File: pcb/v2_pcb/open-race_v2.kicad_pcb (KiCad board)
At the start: 8 copper layers, 90.5 x 49.5 mm, 337 parts, among them IC1 AP33772SDKZ-13-FA02, J1 Conn_ARM_SWD_TagConnect_TC203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, J2 USB4105-GF-A, J20 2S_PACK_BALANCE, J3 DM3CS-SF, J800 M50-3530642 (VTREF sense only), J900 U.FL-R-SMT-1(10), Q1 CSD18540Q5B, Q2 CSD18540Q5B, Q3 CSD18540Q5B, Q4 CSD18540Q5B, Q5 CSD18540Q5B, SW1101 KMR223NG ULC LFG, SW1102 KMR223NG ULC LFG, SW1103 KMR223NG ULC LFG, SW300 KMR223NG ULC LFG, SW301 KMR223NG ULC LFG, SW800 KMR223NG ULC LFG, SW801 KMR223NG ULC LFG, U1 STM32N657X0H3Q, U10 TPSM863253RDXR, U1000 SCH16T-K01-1, U11 TPS22997RYZR, U1100 SN74AHCT1G125DCKR, U1101 SN74AHCT1G125DCKR, U20 TPS630701RNMR (5V fixed), U21 TPS22918DBVR, U22 TPS22918DBVR, U23 TPS22918DBVR, U24 TXS0104EPW, U25 TPS3808G01DBVR, U26 TLV75533PDBVR, U3 APS512XXN-OB9-BG, U4 TPD8S300ARUKR, U5 IS25WP512M-RHLE, U6 BQ25798RQMR, U7 MAX17320G22+, U8 RPL-3.0-R, U800 ESP32-C6-MINI-1, U900 UM980, Y1 NX2016SA-24MHZ-EXS00A-CS10820, Y2 NX2012SA-32.768KHZ-EXS00A-MU0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

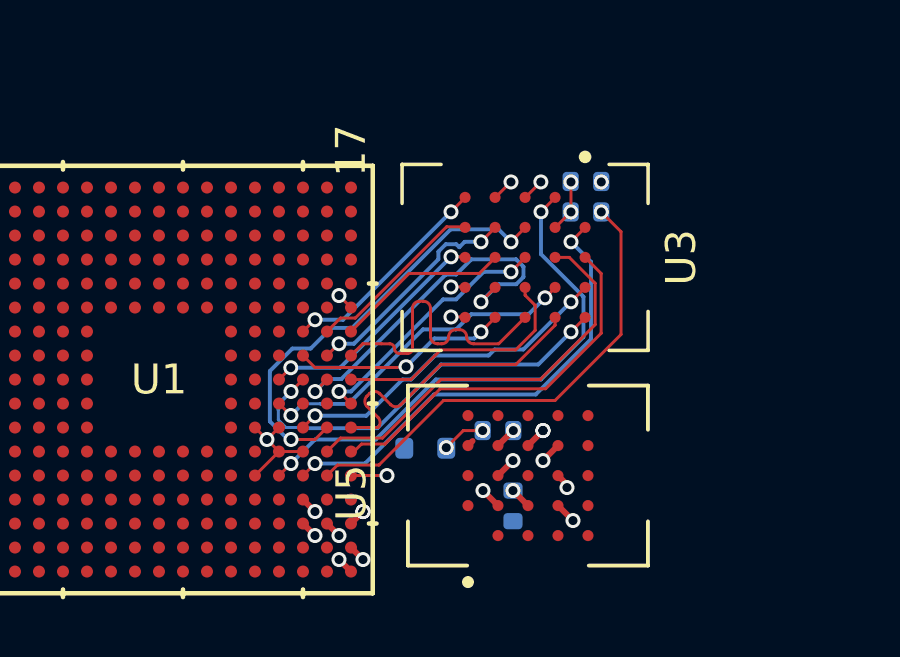
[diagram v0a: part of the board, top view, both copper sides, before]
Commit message: fix top impedence
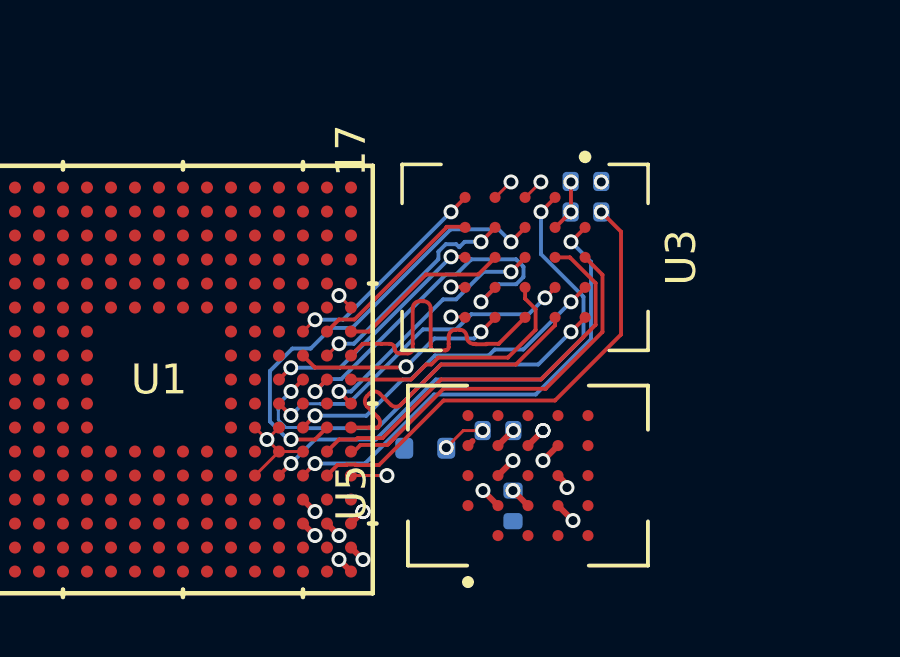
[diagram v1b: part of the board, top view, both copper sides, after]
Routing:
- net /STM32 MCU IO/PSRAM_IO15: track 9.75 -> 10.3 mm

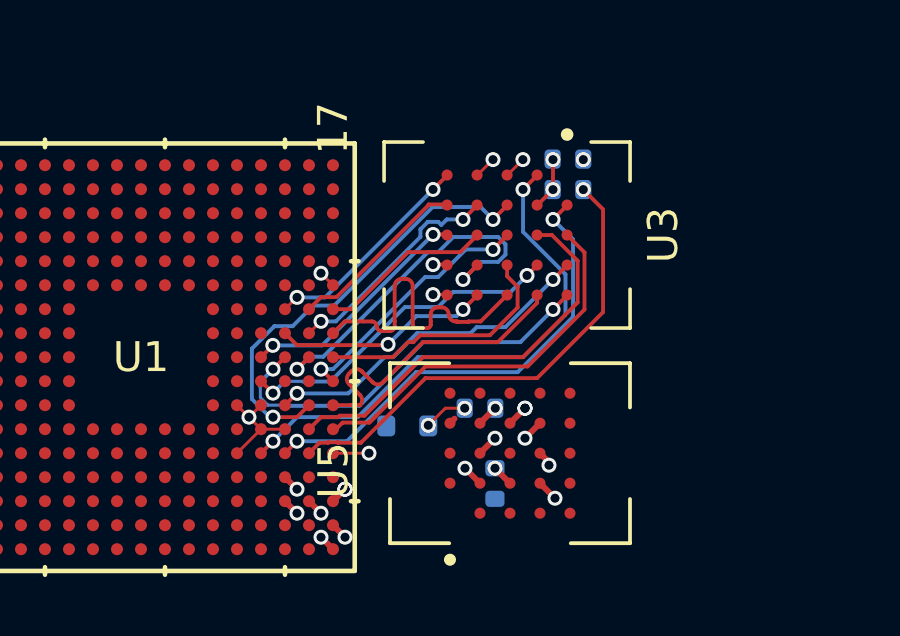
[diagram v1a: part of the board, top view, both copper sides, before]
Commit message: add ground plane
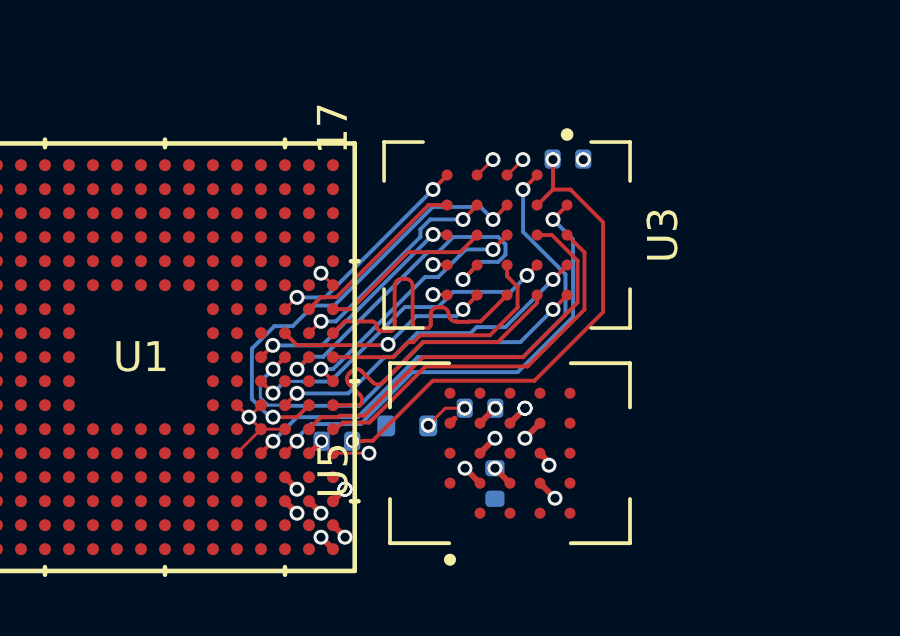
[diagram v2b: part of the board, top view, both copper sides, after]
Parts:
- moved R58 11.4 mm to (128.2, 101.1), turned to 180 degrees
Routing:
- net Net-(U1C-PO4): track 16.1 -> 0.59 mm
- net /STM32 MCU IO/PSRAM_CLK: track 1.70 -> 17.0 mm
- added copper zone on In6.Cu, net GND

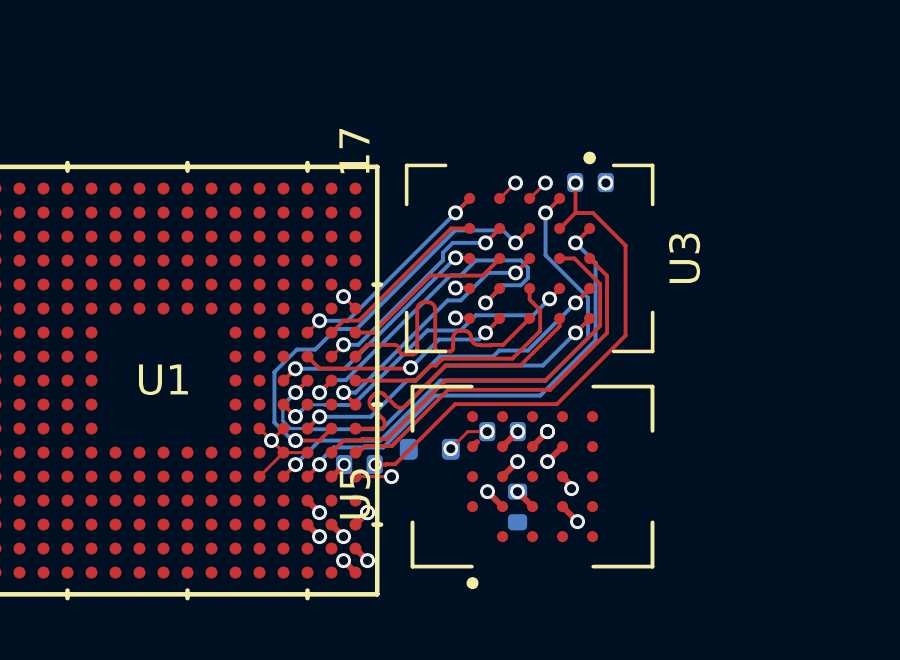
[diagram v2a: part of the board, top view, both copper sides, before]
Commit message: swithc 3to 3 layer signal for ram
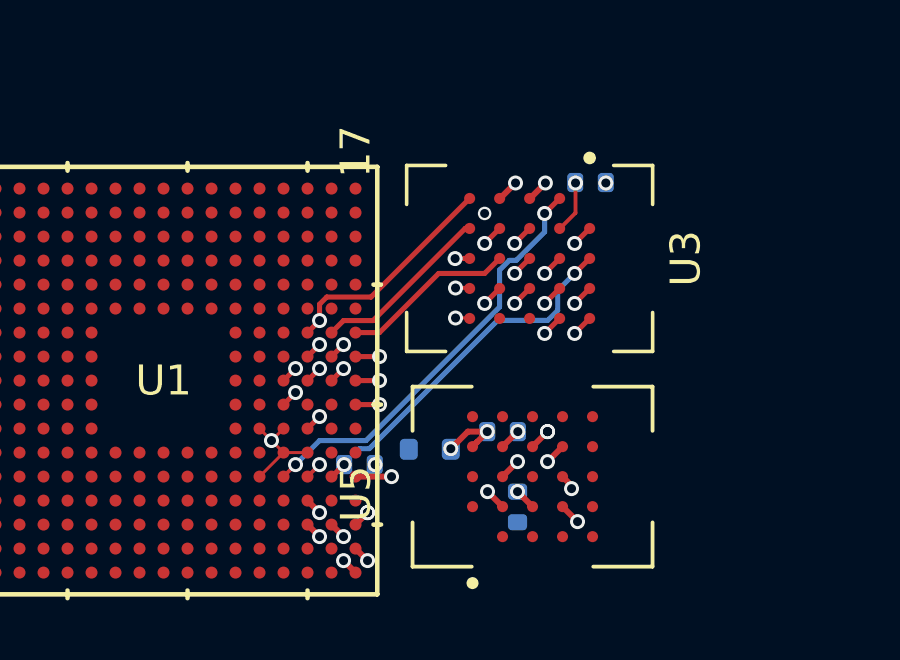
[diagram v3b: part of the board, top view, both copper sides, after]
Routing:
- net /STM32 MCU IO/PSRAM_CLK: track 17.0 -> 1.70 mm
- net /STM32 MCU IO/PSRAM_IO10: track 15.8 -> 1.37 mm
- net /STM32 MCU IO/PSRAM_IO8: track 14.9 -> 0.71 mm, vias 2 -> 1
- net /STM32 MCU IO/PSRAM_DQS1: track 13.8 -> 0.71 mm, vias 0 -> 1
- net /STM32 MCU IO/PSRAM_IO12: track 13.6 -> 1.27 mm
- net /STM32 MCU IO/PSRAM_IO3: track 12.2 -> 1.27 mm
- net /STM32 MCU IO/PSRAM_IO11: track 11.4 -> 1.27 mm
- net /STM32 MCU IO/PSRAM_IO13: track 11.2 -> 1.27 mm
- net /STM32 MCU IO/PSRAM_IO15: track 10.3 -> 0.80 mm, vias 0 -> 1
- net /STM32 MCU IO/PSRAM_IO14: track 10.0 -> 0.71 mm, vias 0 -> 1
- net /STM32 MCU IO/PSRAM_DQS0: track 8.66 -> 1.51 mm
- net /STM32 MCU IO/PSRAM_IO2: track 8.40 -> 1.51 mm, vias 0 -> 2
- net /STM32 MCU IO/PSRAM_IO4: track 7.30 -> 0.57 mm, vias 2 -> 1
- net /STM32 MCU IO/PSRAM_IO1: track 7.56 -> 1.27 mm
- net /STM32 MCU IO/PSRAM_IO9: track 17.5 -> 14.1 mm
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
